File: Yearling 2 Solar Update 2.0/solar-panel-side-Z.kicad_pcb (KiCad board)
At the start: 4 copper layers, 100 x 100 mm, 37 parts, among them J1 CON-5040500591, J2 Screw_Terminal_01x02, J3 Conn_01x01, J4 Conn_01x01, J5 Conn_01x01, J6 Conn_01x01, U1 APDS-9960, U2 DRV2605LDGS, U3 MCP9808_DFN, U4 MCP96L01T-E_MX

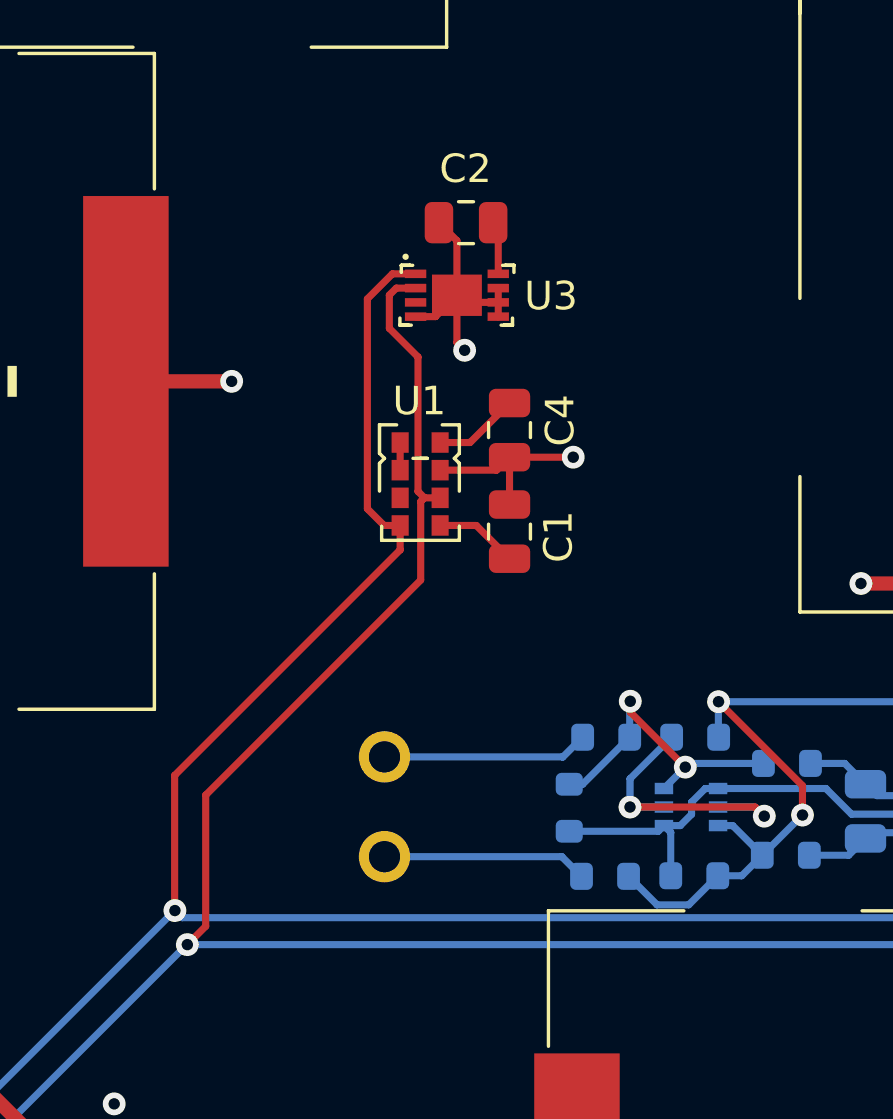
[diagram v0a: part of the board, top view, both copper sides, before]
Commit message: Minor Change to light sensor
Replaced APDS part with VLM. Also added LEDS
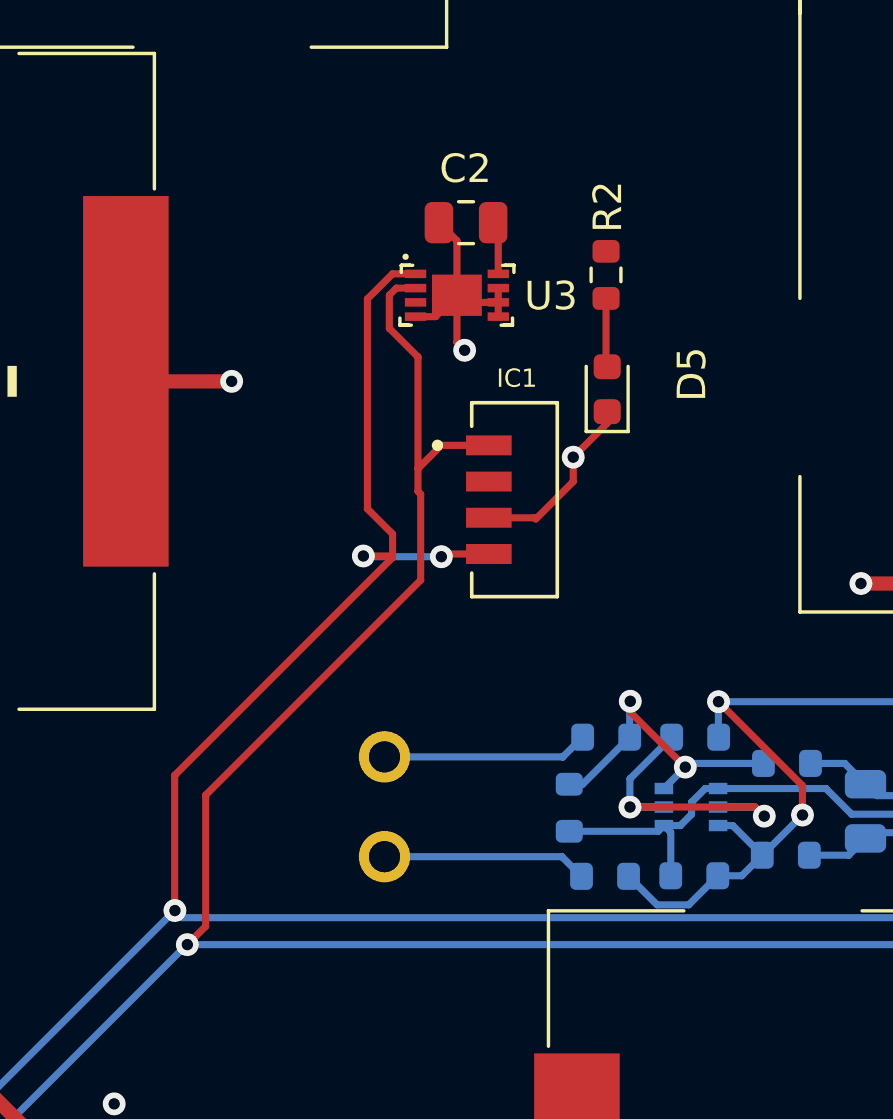
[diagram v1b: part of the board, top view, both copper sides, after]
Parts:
- removed C1, C4: 1uF, Capacitor_SMD:C_0805_2012Metric
- removed U1: APDS-9960, SolarPanelBoards:APDS-9960
- added D5: CQY99, LED_SMD:LED_0603_1608Metric, F.Cu at (158.5, 70.1)
- added IC1: VEML7700, VEML7700-TT:XDCR_VEML7700-TT, F.Cu at (155.2, 74.0)
- added R2: 1k, Resistor_SMD:R_0603_1608Metric, F.Cu at (158.5, 66.1)
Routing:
- net +3V3: track 44.9 -> 38.9 mm
- net SDA: track 94.8 -> 99.7 mm, vias 3 -> 5
- net Net-(D5-Pad2): track 0.00 -> 2.41 mm
- net SCL: track 89.0 -> 91.2 mm
- net Net-(U1-Pad3): track 0.97 -> 0.00 mm

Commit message: Boards as Ordered Jan 31,2023
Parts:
- removed the R2 at (137.3, 101.4)
- removed R7: 10-kOhm, Resistor_SMD:R_0603_1608Metric
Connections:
- U3 pad 6: GND -> +3V3
- U3 pad 7: GND -> +3V3
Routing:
- net +3V3: track 38.9 -> 36.5 mm
- net SDA: track 99.7 -> 97.3 mm, vias 5 -> 4
- net SCL: track 91.2 -> 88.8 mm, vias 3 -> 2
- net GND: track 105.0 -> 104.2 mm, vias 16 -> 12
